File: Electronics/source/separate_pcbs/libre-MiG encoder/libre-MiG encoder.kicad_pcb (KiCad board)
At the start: 2 copper layers, 19 x 19 mm, 2 parts, among them J21 Conn_01x08, SW15 RKJXV1220

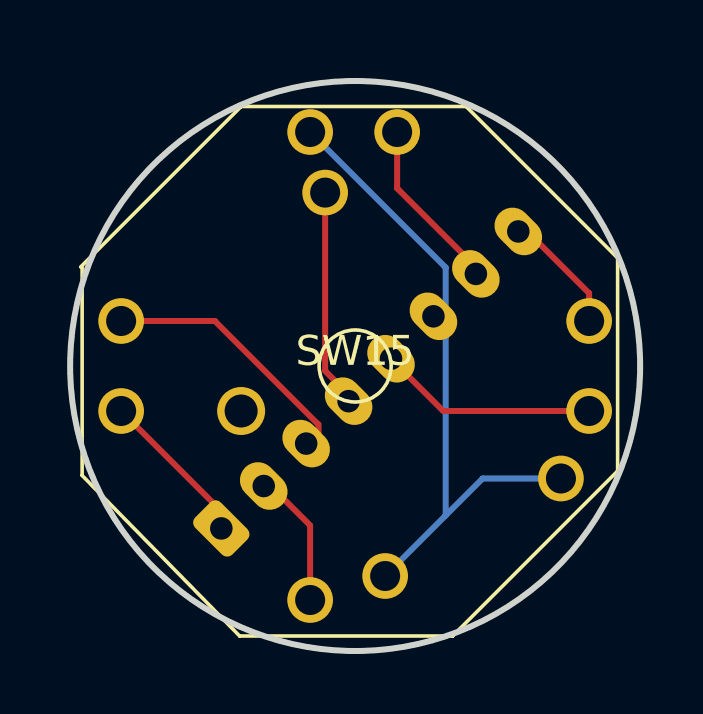
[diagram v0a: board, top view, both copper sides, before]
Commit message: added mechanical ignore
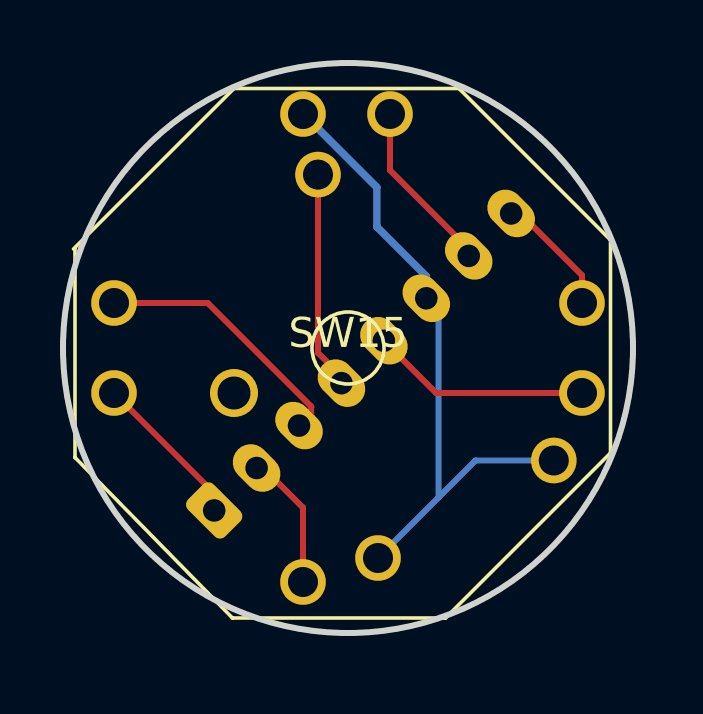
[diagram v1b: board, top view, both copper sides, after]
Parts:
- moved J21 0.65 mm to (111.7, 185.9)
- moved SW15 0.65 mm to (116.2, 180.4)
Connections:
- SW15 pad GND: (no net) -> GND
